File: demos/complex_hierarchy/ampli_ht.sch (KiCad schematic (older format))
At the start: 29 parts, among them P5 CONN_2, P6 CONN_2, Q5 MPAS92, Q6 MPAS42, Q7 MPAS92, Q8 MPAS42, U4 LM358N

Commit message: Update demos
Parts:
- C12, C6, C7, C8: symbol C -> complex_hierarchy_schlib:C
- D5, D6, D7, D8: symbol D_Small -> complex_hierarchy_schlib:D_Small
- P5, P6: symbol CONN_2 -> complex_hierarchy_schlib:CONN_2
- Q5, Q7: symbol MPSA92 -> complex_hierarchy_schlib:MPSA92
- Q6, Q8: symbol MPSA42 -> complex_hierarchy_schlib:MPSA42
- R10, R13, R14, R15, R16, R17, R18, R19, R21, R22, R23, R25, R26: symbol R -> complex_hierarchy_schlib:R
- RV2: symbol POT -> complex_hierarchy_schlib:POT
- U4: symbol LM358N -> complex_hierarchy_schlib:LM358N
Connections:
- net GND: now also Q7.3 (C); no longer Q7.C
- net HT: now also Q6.3 (C); no longer Q6.C
- net at D6.1 (K), R14.1: now also Q5.2 (B); no longer Q5.B
- net at R13.2: now also Q5.1 (E); no longer Q5.E
- net at R15.2, R26.2: now also Q6.1 (E); no longer Q6.E
- net at R19.1: now also Q8.1 (E); no longer Q8.E
- net at R22.2, R25.2: now also Q7.1 (E); no longer Q7.E
- net at R18.1: now also Q8.2 (B); no longer Q8.B
- net at D7.1 (K), R10.1: now also Q7.2 (B), Q8.3 (C); no longer Q7.B, Q8.C
- new net: D8.2 (A), Q5.3 (C), Q6.2 (B)
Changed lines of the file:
@@
-EESchema Schematic File Version 2
-LIBS:power
-LIBS:complex_hierarchy_schlib
+EESchema Schematic File Version 4
 LIBS:complex_hierarchy-cache
 EELAYER 26 0
@@
 Connection ~ 8900 5400
 $Comp
-L R R26
+L complex_hierarchy_schlib:R R26
 U 1 1 4B617B88
 P 9100 5100
@@
 $EndComp
 $Comp
-L R R25
+L complex_hierarchy_schlib:R R25
 U 1 1 4B616B96
 P 9450 4450
@@
 $EndComp
 $Comp
-L D_Small D8
+L complex_hierarchy_schlib:D_Small D8
 U 1 1 4B616AFA
 P 7900 4000
@@
 $EndComp
 $Comp
-L GND #PWR019
+L complex_hierarchy_schlib:GND #PWR019
 U 1 1 4B6168A3
 P 8100 5950
@@
 $EndComp
 $Comp
-L R R10
+L complex_hierarchy_schlib:R R10
 U 1 1 4B61688C
 P 8100 5250
@@
 $EndComp
 $Comp
-L GND #PWR036
+L complex_hierarchy_schlib:GND #PWR036
 U 1 1 4B4F364A
 P 2850 2450
@@
 $EndComp
 $Comp
-L C C12
+L complex_hierarchy_schlib:C C12
 U 1 1 4B4F3641
 P 2850 2250
@@
 $EndComp
 $Comp
-L R R23
+L complex_hierarchy_schlib:R R23
 U 1 1 4B4F363E
 P 2450 2000
@@
 $EndComp
 $Comp
-L -VAA #PWR021
+L complex_hierarchy_schlib:-VAA #PWR021
 U 1 1 4B4B1086
 P 6300 5850
@@
 $EndComp
 $Comp
-L -VAA #PWR022
+L complex_hierarchy_schlib:-VAA #PWR022
 U 1 1 4B4B1080
 P 4750 2850
@@
 Vpil_0_3,3V
 $Comp
-L MPSA42 Q6
+L complex_hierarchy_schlib:MPSA42 Q6
 U 1 1 4B3A137D
 P 8500 3700
@@
 $EndComp
 $Comp
-L MPSA92 Q7
+L complex_hierarchy_schlib:MPSA92 Q7
 U 1 1 4B3A137C
 P 8500 4800
@@
 $EndComp
 $Comp
-L D_Small D7
+L complex_hierarchy_schlib:D_Small D7
 U 1 1 4B3A137B
 P 7900 4500
@@
 $EndComp
 $Comp
-L GND #PWR023
+L complex_hierarchy_schlib:GND #PWR023
 U 1 1 4B3A137A
 P 8600 5300
@@
 $EndComp
 $Comp
-L MPSA42 Q8
+L complex_hierarchy_schlib:MPSA42 Q8
 U 1 1 4B3A1379
 P 7800 5100
@@
 $EndComp
 $Comp
-L GND #PWR024
+L complex_hierarchy_schlib:GND #PWR024
 U 1 1 4B3A1378
 P 7000 5200
@@
 $EndComp
 $Comp
-L D_Small D6
+L complex_hierarchy_schlib:D_Small D6
 U 1 1 4B3A1377
 P 7300 3100
@@
 $EndComp
 $Comp
-L R R13
+L complex_hierarchy_schlib:R R13
 U 1 1 4B3A1376
 P 7900 2750
@@
 $EndComp
 $Comp
-L D_Small D5
+L complex_hierarchy_schlib:D_Small D5
 U 1 1 4B3A1375
 P 7300 2800
@@
 $EndComp
 $Comp
-L R R14
+L complex_hierarchy_schlib:R R14
 U 1 1 4B3A1374
 P 7300 3600
@@
 $EndComp
 $Comp
-L GND #PWR025
+L complex_hierarchy_schlib:GND #PWR025
 U 1 1 4B3A1373
 P 7300 3850
@@
 $EndComp
 $Comp
-L R R18
+L complex_hierarchy_schlib:R R18
 U 1 1 4B3A1371
 P 7250 5100
@@
 $EndComp
 $Comp
-L R R22
+L complex_hierarchy_schlib:R R22
 U 1 1 4B3A1370
 P 8900 5100
@@
 $EndComp
 $Comp
-L +12V #U026
+L complex_hierarchy_schlib:+12V #U026
 U 1 1 4B3A136F
 P 6300 4950
@@
 $EndComp
 $Comp
-L R R19
+L complex_hierarchy_schlib:R R19
 U 1 1 4B3A136D
 P 7400 5400
@@
 $EndComp
 $Comp
-L CONN_2 P5
+L complex_hierarchy_schlib:CONN_2 P5
 U 1 1 4B3A136C
 P 10750 4400
@@
 S_OUT+
 $Comp
-L R R16
+L complex_hierarchy_schlib:R R16
 U 1 1 4B3A136B
 P 3250 2000
@@
 $EndComp
 $Comp
-L GND #PWR027
+L complex_hierarchy_schlib:GND #PWR027
 U 1 1 4B3A136A
 P 1800 2250
@@
 $EndComp
 $Comp
-L GND #PWR028
+L complex_hierarchy_schlib:GND #PWR028
 U 1 1 4B3A1369
 P 4000 2750
@@
 $EndComp
 $Comp
-L LM358N U4
+L complex_hierarchy_schlib:LM358N U4
 U 1 1 4B3A1368
 P 6400 5400
@@
 $EndComp
 $Comp
-L CONN_2 P6
+L complex_hierarchy_schlib:CONN_2 P6
 U 1 1 4B3A1367
 P 1350 2100
@@
 $EndComp
 $Comp
-L C C7
+L complex_hierarchy_schlib:C C7
 U 1 1 4B3A1366
 P 4000 2550
@@
 $EndComp
 $Comp
-L C C8
+L complex_hierarchy_schlib:C C8
 U 1 1 4B3A1365
 P 8100 5750
@@
 $EndComp
 $Comp
-L R R15
+L complex_hierarchy_schlib:R R15
 U 1 1 4B3A1364
 P 9450 4150
@@
 $EndComp
 $Comp
-L GND #PWR029
+L complex_hierarchy_schlib:GND #PWR029
 U 1 1 4B3A1363
 P 10250 4550
@@
 $EndComp
 $Comp
-L R R21
+L complex_hierarchy_schlib:R R21
 U 1 1 4B3A1362
 P 5250 6400
@@
 $EndComp
 $Comp
-L GND #PWR030
+L complex_hierarchy_schlib:GND #PWR030
 U 1 1 4B3A1361
 P 5050 6400
@@
 $EndComp
 $Comp
-L MPSA92 Q5
+L complex_hierarchy_schlib:MPSA92 Q5
 U 1 1 4B3A1360
 P 7800 3300
@@
 $EndComp
 $Comp
-L HT #PWR031
+L complex_hierarchy_schlib:HT #PWR031
 U 1 1 4B3A135F
 P 7300 2650
@@
 $EndComp
 $Comp
-L HT #PWR032
+L complex_hierarchy_schlib:HT #PWR032
 U 1 1 4B3A135E
 P 7900 2550
@@
 $EndComp
 $Comp
-L HT #PWR033
+L complex_hierarchy_schlib:HT #PWR033
 U 1 1 4B3A135D
 P 8600 3300
@@
 $EndComp
 $Comp
-L LM358N U4
+L complex_hierarchy_schlib:LM358N U4
 U 2 1 4B3A135C
 P 4850 2400
@@
 $EndComp
 $Comp
-L +12V #U034
+L complex_hierarchy_schlib:+12V #U034
 U 1 1 4B3A135B
 P 4750 1950
@@
 $EndComp
 $Comp
-L R R17
+L complex_hierarchy_schlib:R R17
 U 1 1 4B3A1359
 P 3950 2000
@@
 $EndComp
 $Comp
-L C C6
+L complex_hierarchy_schlib:C C6
 U 1 1 4B3A1358
 P 4350 1600
@@
 Filter:\nFc =1000Hz
 $Comp
-L POT RV2
+L complex_hierarchy_schlib:POT RV2
 U 1 1 4B3A1357
 P 5850 6400

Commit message: Update demos
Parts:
- C12, C6, C7, C8: footprint Discret:C2 -> Capacitor_THT:C_Disc_D5.0mm_W2.5mm_P5.00mm
- D5, D6, D7, D8: footprint Discret:D3 -> Diode_THT:D_DO-35_SOD27_P7.62mm_Horizontal
- R10, R13, R14, R15, R16, R17, R18, R19, R21, R22, R23, R25, R26: footprint Discret:R3-LARGE_PADS -> Resistor_THT:R_Axial_DIN0204_L3.6mm_D1.6mm_P7.62mm_Horizontal
- U4: footprint Housings_DIP:DIP-8_W7.62mm_LongPads -> Package_DIP:DIP-8_W7.62mm_LongPads

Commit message: Demos update
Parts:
- P5, P6: footprint Connect:bornier2 -> TerminalBlock_Phoenix:TerminalBlock_Phoenix_MKDS-1,5-2-5.08_1x02_P5.08mm_Horizontal

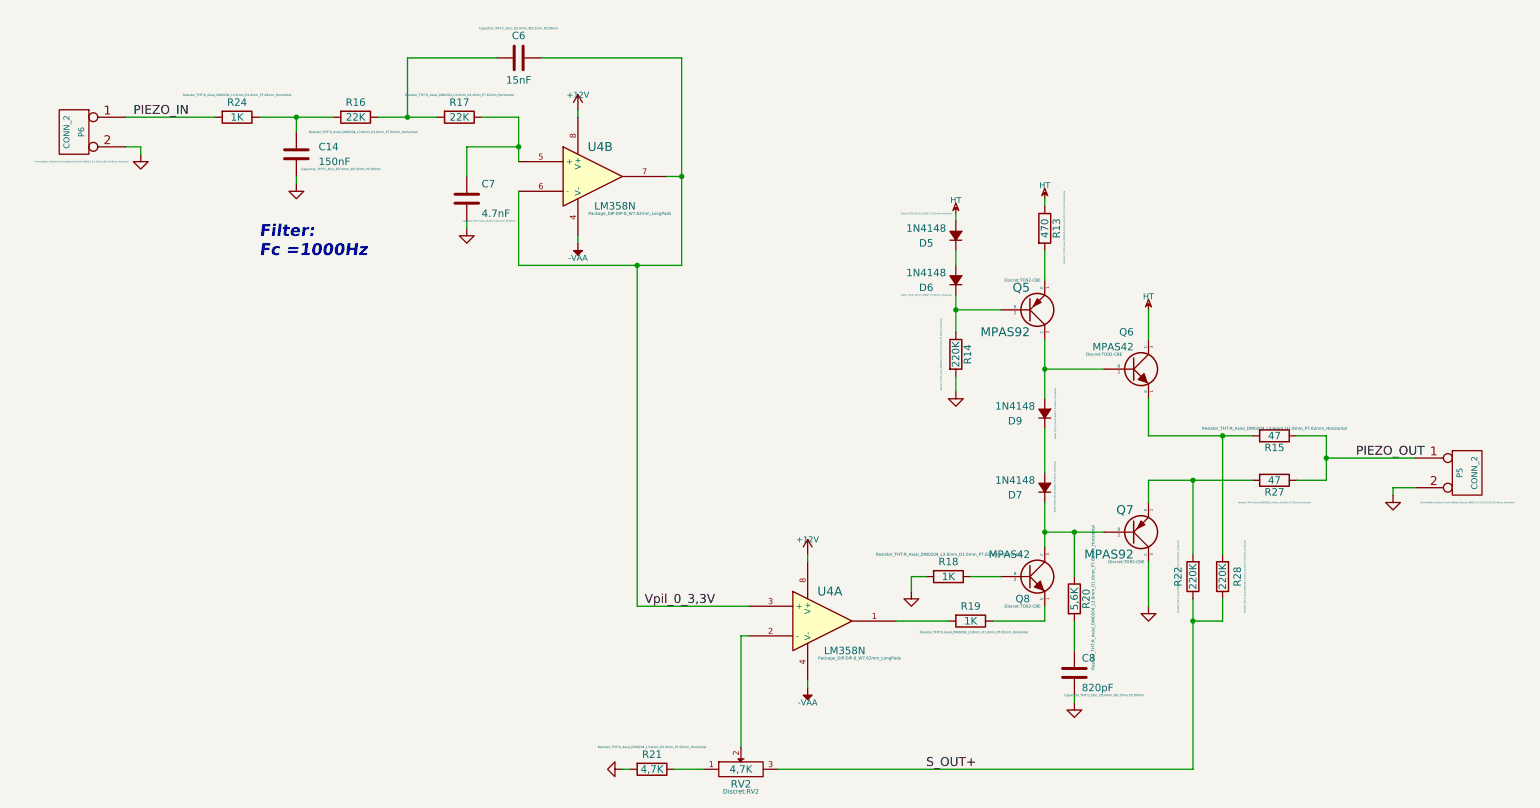
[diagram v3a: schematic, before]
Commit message: Update demos to use recent footprints.
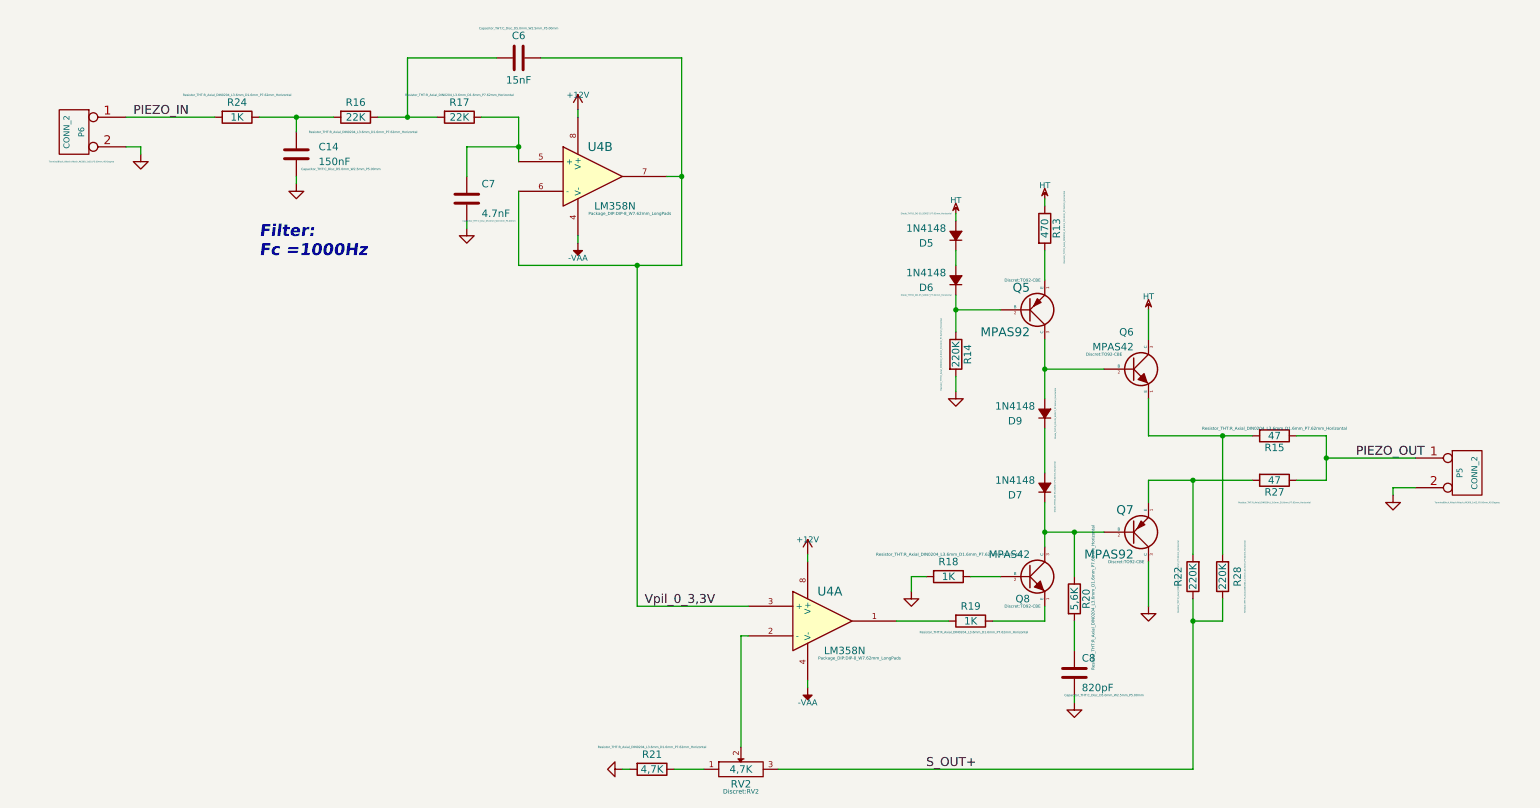
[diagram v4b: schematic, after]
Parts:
- P5, P6: footprint TerminalBlock_Phoenix:TerminalBlock_Phoenix_MKDS-1,5-2-5.08_1x02_P5.08mm_Horizontal -> TerminalBlock_Altech:Altech_AK300_1x02_P5.00mm_45-Degree
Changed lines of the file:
@@
-EESchema Schematic File Version 4
+EESchema Schematic File Version 5
 LIBS:complex_hierarchy-cache
-EELAYER 26 0
+EELAYER 29 0
 EELAYER END
 $Descr A4 11693 8268
@@
 F 0 "P5" V 10700 4400 40  0000 C CNN
 F 1 "CONN_2" V 10800 4400 40  0000 C CNN
-F 2 "TerminalBlock_Phoenix:TerminalBlock_Phoenix_MKDS-1,5-2-5.08_1x02_P5.08mm_Horizontal" H 10750 4200 10  0000 C CNN
+F 2 "TerminalBlock_Altech:Altech_AK300_1x02_P5.00mm_45-Degree" H 10750 4200 10  0000 C CNN
 F 3 "" H 10750 4400 60  0001 C CNN
 	1    10750 4400
@@
 F 0 "P6" V 1300 2100 40  0000 C CNN
 F 1 "CONN_2" V 1400 2100 40  0000 C CNN
-F 2 "TerminalBlock_Phoenix:TerminalBlock_Phoenix_MKDS-1,5-2-5.08_1x02_P5.08mm_Horizontal" H 1300 1900 10  0000 C CNN
+F 2 "TerminalBlock_Altech:Altech_AK300_1x02_P5.00mm_45-Degree" H 1300 1900 10  0000 C CNN
 F 3 "" H 1350 2100 60  0001 C CNN
 	1    1350 2100

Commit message: Demos update
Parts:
- Q5, Q7: value MPAS92 -> MPSA92; footprint Discret:TO92-CBE -> Package_TO_SOT_THT:TO-92_HandSolder
- Q6, Q8: value MPAS42 -> MPSA42; footprint Discret:TO92-CBE -> Package_TO_SOT_THT:TO-92_HandSolder
- RV2: footprint Discret:RV2 -> Potentiometer_THT:Potentiometer_Bourns_3266W_Vertical
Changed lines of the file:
@@
 EESchema Schematic File Version 5
-LIBS:complex_hierarchy-cache
-EELAYER 29 0
+EELAYER 30 0
 EELAYER END
 $Descr A4 11693 8268
@@
 Comment3 ""
 Comment4 ""
+Comment5 ""
+Comment6 ""
+Comment7 ""
+Comment8 ""
+Comment9 ""
 $EndDescr
 Wire Wire Line
@@
 F 0 "#PWR019" H 8100 5950 30  0001 C CNN
 F 1 "GND" H 8100 5880 30  0001 C CNN
-F 2 "" H 8100 5950 60  0001 C CNN
+F 2 "" H 8100 5950 10  0001 C CNN
 F 3 "" H 8100 5950 60  0001 C CNN
 	1    8100 5950
@@
 F 0 "R20" V 8180 5250 50  0000 C CNN
 F 1 "5,6K" V 8100 5250 50  0000 C CNN
-F 2 "Resistor_THT:R_Axial_DIN0204_L3.6mm_D1.6mm_P7.62mm_Horizontal" V 8226 5259 20  0000 C CNN
+F 2 "Resistor_THT:R_Axial_DIN0204_L3.6mm_D1.6mm_P7.62mm_Horizontal" V 8226 5259 10  0000 C CNN
 F 3 "" H 8100 5250 60  0001 C CNN
 	1    8100 5250
@@
 F 0 "#PWR020" H 2850 2450 30  0001 C CNN
 F 1 "GND" H 2850 2380 30  0001 C CNN
-F 2 "" H 2850 2450 60  0001 C CNN
+F 2 "" H 2850 2450 10  0001 C CNN
 F 3 "" H 2850 2450 60  0001 C CNN
 	1    2850 2450
@@
 F 0 "C14" H 3000 2300 50  0000 L CNN
 F 1 "150nF" H 3000 2200 50  0000 L CNN
-F 2 "Capacitor_THT:C_Disc_D5.0mm_W2.5mm_P5.00mm" H 3150 2150 15  0000 C CNN
+F 2 "Capacitor_THT:C_Disc_D5.0mm_W2.5mm_P5.00mm" H 3150 2150 10  0000 C CNN
 F 3 "" H 2850 2250 60  0001 C CNN
 	1    2850 2250
@@
 F 0 "R24" V 2350 2000 50  0000 C CNN
 F 1 "1K" V 2450 2000 50  0000 C CNN
-F 2 "Resistor_THT:R_Axial_DIN0204_L3.6mm_D1.6mm_P7.62mm_Horizontal" V 2300 2000 15  0000 C CNN
+F 2 "Resistor_THT:R_Axial_DIN0204_L3.6mm_D1.6mm_P7.62mm_Horizontal" V 2300 2000 10  0000 C CNN
 F 3 "" H 2450 2000 60  0001 C CNN
 	1    2450 2000
@@
 F 0 "#PWR021" H 6300 5950 20  0001 C CNN
 F 1 "-VAA" H 6300 5950 40  0000 C CNN
-F 2 "" H 6300 5850 60  0001 C CNN
+F 2 "" H 6300 5850 10  0001 C CNN
 F 3 "" H 6300 5850 60  0001 C CNN
 	1    6300 5850
@@
 F 0 "#PWR022" H 4750 2950 20  0001 C CNN
 F 1 "-VAA" H 4750 2950 40  0000 C CNN
-F 2 "" H 4750 2850 60  0001 C CNN
+F 2 "" H 4750 2850 10  0001 C CNN
 F 3 "" H 4750 2850 60  0001 C CNN
 	1    4750 2850
@@
 AR Path="/4B3A1333/4B3A137D" Ref="Q2"  Part="1"
 F 0 "Q6" H 8500 3950 50  0000 R CNN
-F 1 "MPAS42" H 8500 3850 50  0000 R CNN
-F 2 "Discret:TO92-CBE" H 8300 3800 20  0000 C CNN
+F 1 "MPSA42" H 8500 3850 50  0000 R CNN
+F 2 "Package_TO_SOT_THT:TO-92_HandSolder" H 8300 3800 10  0000 C CNN
 F 3 "" H 8500 3700 60  0001 C CNN
 	1    8500 3700
@@
 AR Path="/4B3A1333/4B3A137C" Ref="Q3"  Part="1"
 F 0 "Q7" H 8500 4650 60  0000 R CNN
-F 1 "MPAS92" H 8500 4950 60  0000 R CNN
-F 2 "Discret:TO92-CBE" H 8450 5000 20  0000 C CNN
+F 1 "MPSA92" H 8500 4950 60  0000 R CNN
+F 2 "Package_TO_SOT_THT:TO-92_HandSolder" H 8450 5000 10  0000 C CNN
 F 3 "" H 8500 4800 60  0001 C CNN
 	1    8500 4800
@@
 F 0 "#PWR023" H 8600 5300 30  0001 C CNN
 F 1 "GND" H 8600 5230 30  0001 C CNN
-F 2 "" H 8600 5300 60  0001 C CNN
+F 2 "" H 8600 5300 10  0001 C CNN
 F 3 "" H 8600 5300 60  0001 C CNN
 	1    8600 5300
@@
 AR Path="/4B3A1333/4B3A1379" Ref="Q4"  Part="1"
 F 0 "Q8" H 7800 4950 50  0000 R CNN
-F 1 "MPAS42" H 7800 5250 50  0000 R CNN
-F 2 "Discret:TO92-CBE" H 7750 4900 20  0000 C CNN
+F 1 "MPSA42" H 7800 5250 50  0000 R CNN
+F 2 "Package_TO_SOT_THT:TO-92_HandSolder" H 7750 4900 10  0000 C CNN
 F 3 "" H 7800 5100 60  0001 C CNN
 	1    7800 5100
@@
 F 0 "#PWR024" H 7000 5200 30  0001 C CNN
 F 1 "GND" H 7000 5130 30  0001 C CNN
-F 2 "" H 7000 5200 60  0001 C CNN
+F 2 "" H 7000 5200 10  0001 C CNN
 F 3 "" H 7000 5200 60  0001 C CNN
 	1    7000 5200
@@
 F 0 "#PWR025" H 7300 3850 30  0001 C CNN
 F 1 "GND" H 7300 3780 30  0001 C CNN
-F 2 "" H 7300 3850 60  0001 C CNN
+F 2 "" H 7300 3850 10  0001 C CNN
 F 3 "" H 7300 3850 60  0001 C CNN
 	1    7300 3850
@@
 F 0 "R18" V 7150 5100 50  0000 C CNN
 F 1 "1K" V 7250 5100 50  0000 C CNN
-F 2 "Resistor_THT:R_Axial_DIN0204_L3.6mm_D1.6mm_P7.62mm_Horizontal" V 7100 5100 20  0000 C CNN
+F 2 "Resistor_THT:R_Axial_DIN0204_L3.6mm_D1.6mm_P7.62mm_Horizontal" V 7100 5100 10  0000 C CNN
 F 3 "" H 7250 5100 60  0001 C CNN
 	1    7250 5100
@@
 F 0 "#U026" H 6300 4900 20  0001 C CNN
 F 1 "+12V" H 6300 5050 40  0000 C CNN
-F 2 "" H 6300 4950 60  0001 C CNN
+F 2 "" H 6300 4950 10  0001 C CNN
 F 3 "" H 6300 4950 60  0001 C CNN
 	1    6300 4950
@@
 F 0 "R19" V 7300 5400 50  0000 C CNN
 F 1 "1K" V 7400 5400 50  0000 C CNN
-F 2 "Resistor_THT:R_Axial_DIN0204_L3.6mm_D1.6mm_P7.62mm_Horizontal" V 7475 5422 15  0000 C CNN
+F 2 "Resistor_THT:R_Axial_DIN0204_L3.6mm_D1.6mm_P7.62mm_Horizontal" V 7475 5422 10  0000 C CNN
 F 3 "" H 7400 5400 60  0001 C CNN
 	1    7400 5400
@@
 F 0 "R16" V 3150 2000 50  0000 C CNN
 F 1 "22K" V 3250 2000 50  0000 C CNN
-F 2 "Resistor_THT:R_Axial_DIN0204_L3.6mm_D1.6mm_P7.62mm_Horizontal" V 3350 2050 15  0000 C CNN
+F 2 "Resistor_THT:R_Axial_DIN0204_L3.6mm_D1.6mm_P7.62mm_Horizontal" V 3350 2050 10  0000 C CNN
 F 3 "" H 3250 2000 60  0001 C CNN
 	1    3250 2000
@@
 F 0 "#PWR027" H 1800 2250 30  0001 C CNN
 F 1 "GND" H 1800 2180 30  0001 C CNN
-F 2 "" H 1800 2250 60  0001 C CNN
+F 2 "" H 1800 2250 10  0001 C CNN
 F 3 "" H 1800 2250 60  0001 C CNN
 	1    1800 2250
@@
 F 0 "#PWR028" H 4000 2750 30  0001 C CNN
 F 1 "GND" H 4000 2680 30  0001 C CNN
-F 2 "" H 4000 2750 60  0001 C CNN
+F 2 "" H 4000 2750 10  0001 C CNN
 F 3 "" H 4000 2750 60  0001 C CNN
 	1    4000 2750
@@
 F 0 "U4" H 6450 5600 60  0000 C CNN
 F 1 "LM358N" H 6550 5200 50  0000 C CNN
-F 2 "Package_DIP:DIP-8_W7.62mm_LongPads" H 6650 5150 20  0000 C CNN
+F 2 "Package_DIP:DIP-8_W7.62mm_LongPads" H 6650 5150 10  0000 C CNN
 F 3 "" H 6400 5400 60  0001 C CNN
 	1    6400 5400
@@
 F 0 "C8" H 8150 5850 50  0000 L CNN
 F 1 "820pF" H 8150 5650 50  0000 L CNN
-F 2 "Capacitor_THT:C_Disc_D5.0mm_W2.5mm_P5.00mm" H 8300 5600 15  0000 C CNN
+F 2 "Capacitor_THT:C_Disc_D5.0mm_W2.5mm_P5.00mm" H 8300 5600 10  0000 C CNN
 F 3 "" H 8100 5750 60  0001 C CNN
 	1    8100 5750
@@
 F 0 "R15" V 9530 4150 50  0000 C CNN
 F 1 "47" V 9450 4150 50  0000 C CNN
-F 2 "Resistor_THT:R_Axial_DIN0204_L3.6mm_D1.6mm_P7.62mm_Horizontal" V 9400 4150 20  0000 C CNN
+F 2 "Resistor_THT:R_Axial_DIN0204_L3.6mm_D1.6mm_P7.62mm_Horizontal" V 9400 4150 10  0000 C CNN
 F 3 "" H 9450 4150 60  0001 C CNN
 	1    9450 4150
@@
 F 0 "#PWR029" H 10250 4550 30  0001 C CNN
 F 1 "GND" H 10250 4480 30  0001 C CNN
-F 2 "" H 10250 4550 60  0001 C CNN
+F 2 "" H 10250 4550 10  0001 C CNN
 F 3 "" H 10250 4550 60  0001 C CNN
 	1    10250 4550
@@
 F 0 "R21" V 5150 6400 50  0000 C CNN
 F 1 "4,7K" V 5250 6400 50  0000 C CNN
-F 2 "Resistor_THT:R_Axial_DIN0204_L3.6mm_D1.6mm_P7.62mm_Horizontal" V 5100 6400 15  0000 C CNN
+F 2 "Resistor_THT:R_Axial_DIN0204_L3.6mm_D1.6mm_P7.62mm_Horizontal" V 5100 6400 10  0000 C CNN
 F 3 "" H 5250 6400 60  0001 C CNN
 	1    5250 6400
@@
 F 0 "#PWR030" H 5050 6400 30  0001 C CNN
 F 1 "GND" H 5050 6330 30  0001 C CNN
-F 2 "" H 5050 6400 60  0001 C CNN
+F 2 "" H 5050 6400 10  0001 C CNN
 F 3 "" H 5050 6400 60  0001 C CNN
 	1    5050 6400
@@
 AR Path="/4B3A1333/4B3A1360" Ref="Q1"  Part="1"
 F 0 "Q5" H 7800 3150 60  0000 R CNN
-F 1 "MPAS92" H 7800 3450 60  0000 R CNN
-F 2 "Discret:TO92-CBE" H 7750 3100 20  0000 C CNN
+F 1 "MPSA92" H 7800 3450 60  0000 R CNN
+F 2 "Package_TO_SOT_THT:TO-92_HandSolder" H 7750 3100 10  0000 C CNN
 F 3 "" H 7800 3300 60  0001 C CNN
 	1    7800 3300
@@
 F 0 "#PWR031" H 7300 2770 20  0001 C CNN
 F 1 "HT" H 7300 2740 40  0000 C CNN
-F 2 "" H 7300 2650 60  0001 C CNN
+F 2 "" H 7300 2650 10  0001 C CNN
 F 3 "" H 7300 2650 60  0001 C CNN
 	1    7300 2650
@@
 F 0 "#PWR032" H 7900 2670 20  0001 C CNN
 F 1 "HT" H 7900 2640 40  0000 C CNN
-F 2 "" H 7900 2550 60  0001 C CNN
+F 2 "" H 7900 2550 10  0001 C CNN
 F 3 "" H 7900 2550 60  0001 C CNN
 	1    7900 2550
@@
 F 0 "#PWR033" H 8600 3420 20  0001 C CNN
 F 1 "HT" H 8600 3390 40  0000 C CNN
-F 2 "" H 8600 3300 60  0001 C CNN
+F 2 "" H 8600 3300 10  0001 C CNN
 F 3 "" H 8600 3300 60  0001 C CNN
 	1    8600 3300
@@
 F 0 "U4" H 4900 2600 60  0000 C CNN
 F 1 "LM358N" H 5000 2200 50  0000 C CNN
-F 2 "Package_DIP:DIP-8_W7.62mm_LongPads" H 5100 2150 20  0000 C CNN
+F 2 "Package_DIP:DIP-8_W7.62mm_LongPads" H 5100 2150 10  0000 C CNN
 F 3 "" H 4850 2400 60  0001 C CNN
 	2    4850 2400
@@
 F 0 "#U034" H 4750 1900 20  0001 C CNN
 F 1 "+12V" H 4750 2050 40  0000 C CNN
-F 2 "" H 4750 1950 60  0001 C CNN
+F 2 "" H 4750 1950 10  0001 C CNN
 F 3 "" H 4750 1950 60  0001 C CNN
 	1    4750 1950
@@
 F 0 "R17" V 3850 2000 50  0000 C CNN
 F 1 "22K" V 3950 2000 50  0000 C CNN
-F 2 "Resistor_THT:R_Axial_DIN0204_L3.6mm_D1.6mm_P7.62mm_Horizontal" V 3800 2000 15  0000 C CNN
+F 2 "Resistor_THT:R_Axial_DIN0204_L3.6mm_D1.6mm_P7.62mm_Horizontal" V 3800 2000 10  0000 C CNN
 F 3 "" H 3950 2000 60  0001 C CNN
 	1    3950 2000
@@
 F 0 "C6" V 4200 1600 50  0000 C CNN
 F 1 "15nF" V 4500 1600 50  0000 C CNN
-F 2 "Capacitor_THT:C_Disc_D5.0mm_W2.5mm_P5.00mm" V 4150 1600 15  0000 C CNN
+F 2 "Capacitor_THT:C_Disc_D5.0mm_W2.5mm_P5.00mm" V 4150 1600 10  0000 C CNN
 F 3 "" H 4350 1600 60  0001 C CNN
 	1    4350 1600
@@
 F 0 "RV2" H 5850 6300 50  0000 C CNN
 F 1 "4,7K" H 5850 6400 50  0000 C CNN
-F 2 "Discret:RV2" H 5850 6250 30  0000 C CNN
+F 2 "Potentiometer_THT:Potentiometer_Bourns_3266W_Vertical" H 5850 6250 10  0000 C CNN
 F 3 "" H 5850 6400 60  0001 C CNN
 	1    5850 6400
